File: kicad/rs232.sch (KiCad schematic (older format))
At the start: 16 parts, among them J7 XCVR_CAT_RS232, U8 MAX3387ECUG+

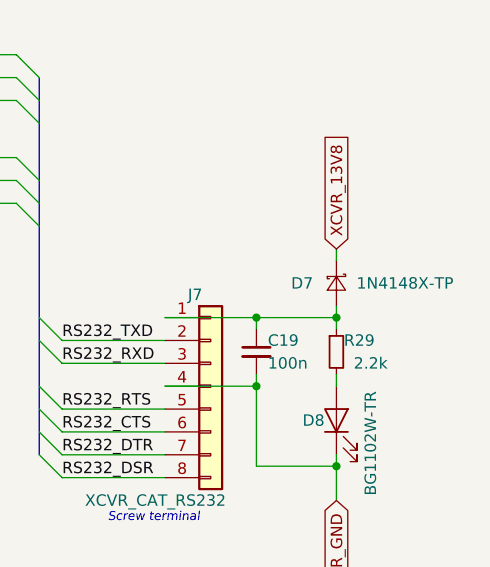
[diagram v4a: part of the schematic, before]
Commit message: Small fixes
* Moved via that was unreasonably close to another one
* Changed 13V8 diodes to SM5819PL-TP
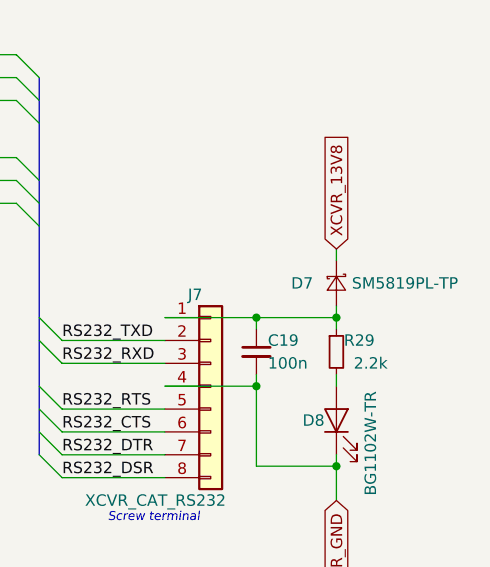
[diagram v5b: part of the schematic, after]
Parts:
- D7: value 1N4148X-TP -> SM5819PL-TP; footprint Diode_SMD:D_SOD-523 -> Diode_SMD:D_SOD-123F
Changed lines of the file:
@@
 AR Path="/5F9E7705/606D9B1D/6072AD2D" Ref="D7"  Part="1"
 F 0 "D7" V 8800 3700 50  0000 C CNN
-F 1 "1N4148X-TP" V 8800 4150 50  0000 C CNN
-F 2 "Diode_SMD:D_SOD-523" V 8800 3850 50  0001 C CNN
+F 1 "SM5819PL-TP" V 8800 4150 50  0000 C CNN
+F 2 "Diode_SMD:D_SOD-123F" V 8800 3850 50  0001 C CNN
 F 3 "~" V 8800 3850 50  0001 C CNN
 	1    8800 3850
